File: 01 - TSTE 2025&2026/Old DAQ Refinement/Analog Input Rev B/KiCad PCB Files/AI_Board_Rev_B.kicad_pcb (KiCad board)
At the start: 2 copper layers, 130 x 165 mm, 54 parts, among them J1 DC37_Socket_MountingHoles, J10 AI4 M12, J11 AI4 XT30, J12 AI5 M12, J13 AI5 XT30, J14 AI6 M12, J15 AI6 XT30, J16 AI7 M12, J17 AI7 XT30, J18 AI8 M12, J19 AI8 XT30, J2 AI0 M12, J20 AI9 M12, J21 AI9 XT30, J22 AI10 M12, J23 AI10 XT30, J24 AI11 M12, J25 AI11 XT30, J26 AI12 M12, J27 AI12 XT30, J28 AI13 M12, J29 AI13 XT30, J3 AI0 XT30, J30 AI14 M12, J31 AI14 XT30, J32 AI15 M12, J33 AI15 XT30, J4 AI1 M12, J5 AI1 XT30, J6 AI2 M12, J7 AI2 XT30, J8 AI3 M12, J9 AI3 XT30, M3 MountingHole_3.2mm_M3

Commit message: Final Files
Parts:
- moved G*** 3.48 mm to (28.1, 152.1)
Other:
- outline, holes or cut-outs redrawn
- board text added: "October 2025"

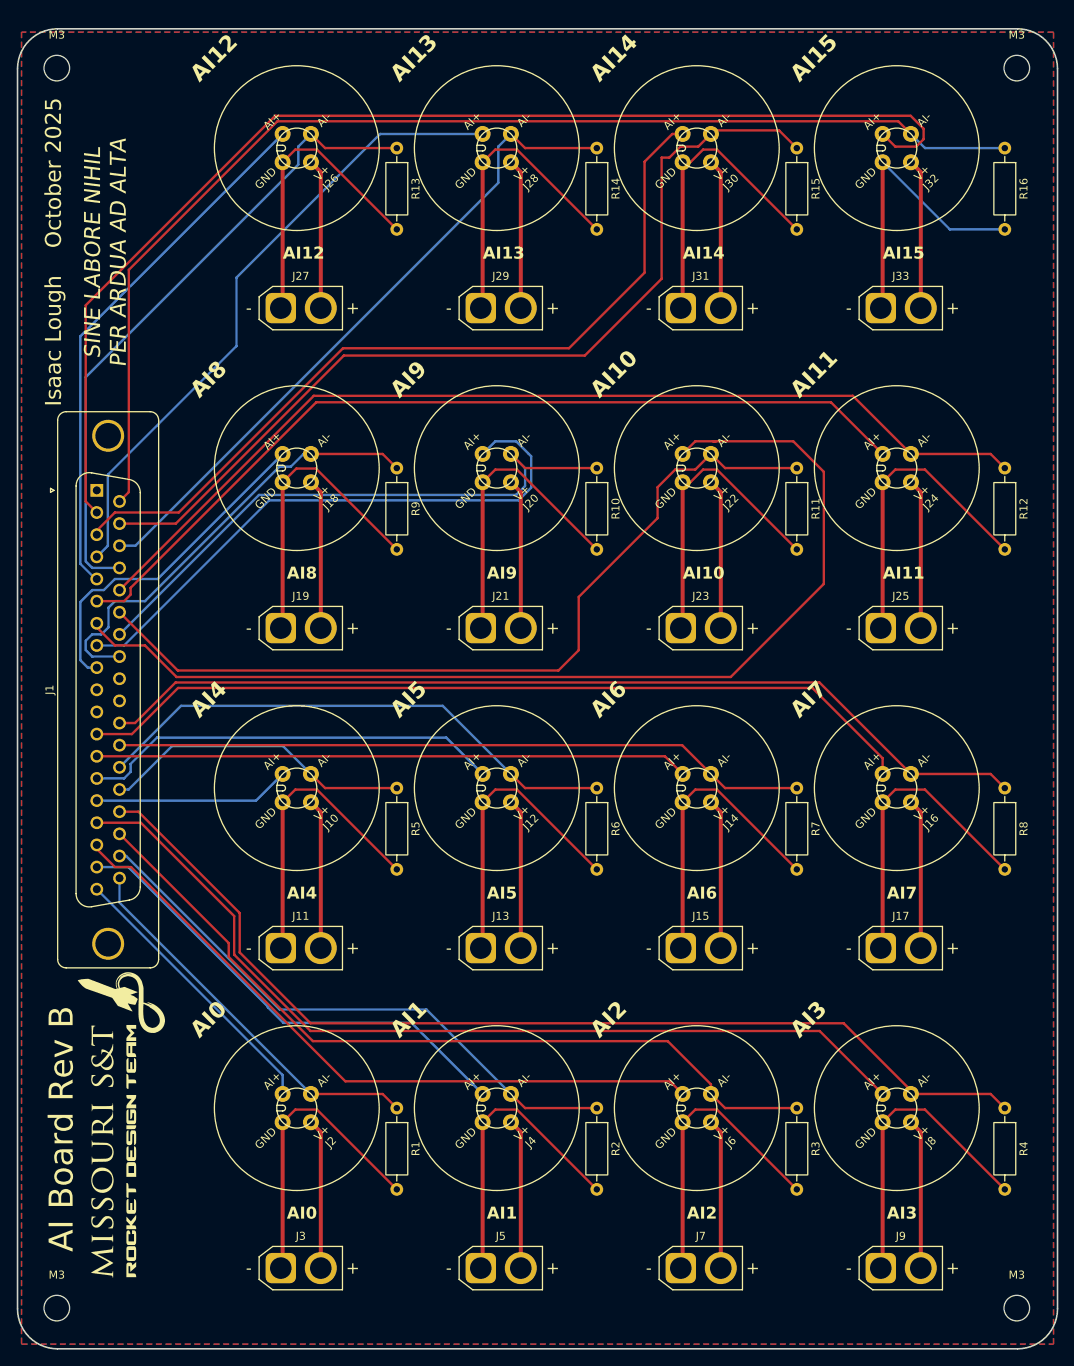
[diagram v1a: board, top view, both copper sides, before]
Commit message: Vias Change Upload
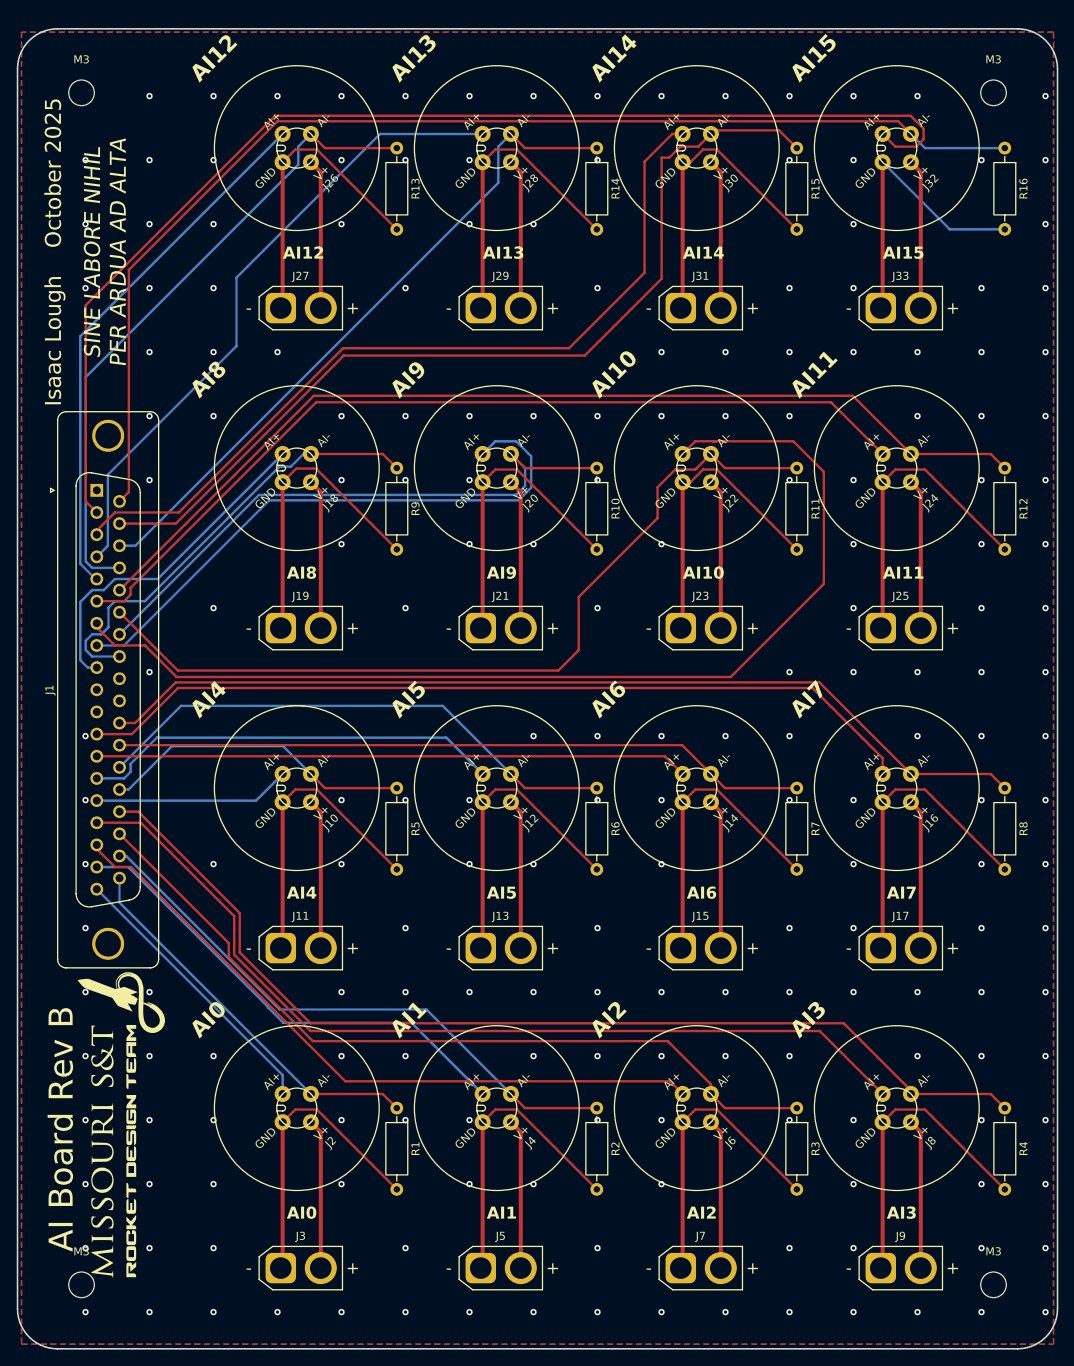
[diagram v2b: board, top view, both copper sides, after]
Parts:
- moved M3 4.37 mm to (23.1, 23.1)
- moved M3 4.24 mm to (137.1, 23.1)
- moved M3 4.24 mm to (23.1, 172.1)
- moved M3 4.11 mm to (137.1, 172.1)
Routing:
- net GND: vias 0 -> 202
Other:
- board text added: "{ "ViaStitching": "0.2", "stitch_zone_0": { "HSpacing": "3", "VSpacing": "3", "HOffset": "0", "VOffset": "0", "Clearance": "0.2", "Randomize": false } }"
- board text added: "{ "ViaStitching": "0.2", "stitch_zone_0": { "HSpacing": "5", "VSpacing": "5", "HOffset": "0", "VOffset": "0", "Clearance": "0.2", "Randomize": false } }"
- board text added: "{ "ViaStitching": "0.2", "stitch_zone_0": { "HSpacing": "8", "VSpacing": "8", "HOffset": "0", "VOffset": "0", "Clearance": "0.2", "Randomize": false } }"
